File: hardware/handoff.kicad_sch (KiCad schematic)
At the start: 67 parts, among them J1 BAT XH-2, J2 PAD JST-XH 2p, J3 LED JST-XH 4p / 5mm RGB, J5 CHG XH-2, SW1 SS-12F23G5, SW2 TACT 6x6, U1 Raspberry Pi Pico 2 W, U2 MCP6292-E/MS

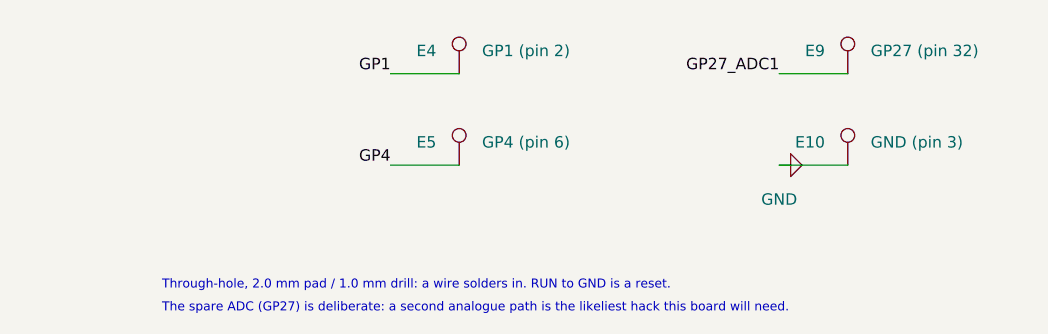
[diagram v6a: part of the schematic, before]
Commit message: Create the PCB: outline, placement, pours, and what would not route
tools/gen_pcb.py is to handoff.kicad_pcb what gen_schematic.py is to the sheet -
the board is regenerated from scratch every run, from the schematic's netlist
and the floor plan, and proved with kicad-cli. It ends DRC 0 errors apart from
the unrouted count and schematic parity 0. Its frame is the floor plan's, one to
one, so every coordinate in it reads straight off floorplan.svg.

Placement is declarative: each part names an anchor - its origin or one of its
pads - and a target, and the script solves for the footprint position. No offset
arithmetic in the table, and a footprint that changes shape cannot quietly drag
a part off its target.

40 x 62 mm, two layers, GND pour on both faces with the TOP pour as the
electrode. The cell/pad pocket is a real rule area barring bottom-face pour and
bottom-face parts, and each mounting hole carries its own 8 mm boss keep-out, so
DRC enforces both rather than a reviewer remembering them.

Two custom DRC rules, both about height, which KiCad does not model: the Pico is
socketed 8.5 mm up so parts may sit under it, and E1-E10 are bare pads whose
inherited courtyard is wider than the pitch they sit on. Both suppress courtyard
overlap only; every clearance and short test still runs.

**The finding: the AFE channel is over-subscribed.** The floor plan puts the AFE
and ten breakout pads in the same 10 mm channel. Measured off the footprints
that is 14.5 mm of parts across 10 mm of width, and what is left is no routing
lane - R2's pad stops 0.225 mm short of U2's pin-1 pad, and each 1206 column
clears U2 by 1.2 mm, one track wide. So stage 1's feedback, OUT1's hop from pin
1, VREF's lower half, AFE_3V3, ADC0 and the JP3/JP6 legs are not routed: 27
unconnected items. That is a placement problem, not a routing problem, and it is
left open rather than bodged with vias through the electrode pour, which is the
one thing that pour cannot afford. Three ways out are written 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
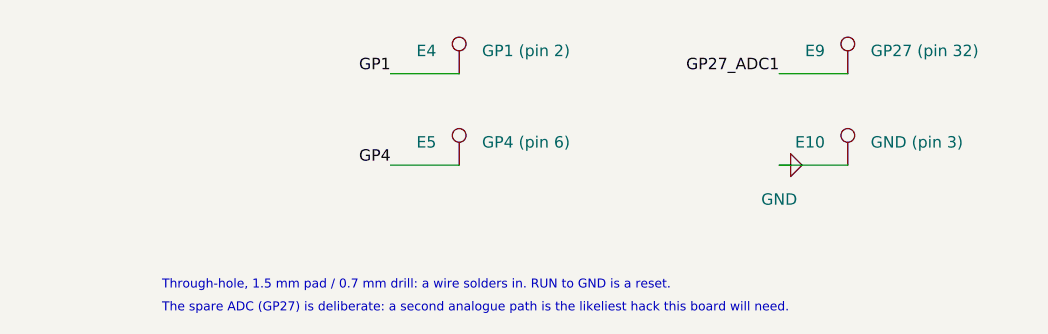
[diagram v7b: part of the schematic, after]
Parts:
- E1, E10, E2, E3, E4, E5, E6, E7, E8, E9: footprint TestPoint:TestPoint_THTPad_D2.0mm_Drill1.0mm -> TestPoint:TestPoint_THTPad_D1.5mm_Drill0.7mm; now left out of the parts list
- JP1, JP2, JP3, JP4, JP5, JP6, JP7, JP8, TP1, TP10, TP11, TP12, TP13, TP2, TP3, TP4, TP5, TP6, TP7, TP8, TP9: now left out of the parts list
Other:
- note added: "Through-hole, 1.5 mm pad / 0.7 mm drill: a wire solders in. RUN to GND is a reset."
- note removed: "Through-hole, 2.0 mm pad / 1.0 mm drill: a wire solders in. RUN to GND is a reset."
